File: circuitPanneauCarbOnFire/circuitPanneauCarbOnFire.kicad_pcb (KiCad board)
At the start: 2 copper layers, 13 parts, among them SW1 SW_DIP_x01, SW2 SW_DIP_x01

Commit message: fichier gerber
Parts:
- added ?: MountingHole_2.7mm_M2.5, MountingHole:MountingHole_2.7mm_M2.5, F.Cu at (86.4, 125.7)
- added ?: MountingHole_2.7mm_M2.5, MountingHole:MountingHole_2.7mm_M2.5, F.Cu at (86.4, 86.4)
- added ?: MountingHole_2.7mm_M2.5, MountingHole:MountingHole_2.7mm_M2.5, F.Cu at (119.4, 125.7)
- added ?: MountingHole_2.7mm_M2.5, MountingHole:MountingHole_2.7mm_M2.5, F.Cu at (119.4, 86.4)
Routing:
- net Net-(C1-Pad1): track 46.6 -> 52.0 mm
- net Net-(D1-Pad1): track 47.7 -> 52.3 mm
- net Net-(R1-Pad1): track 56.2 -> 60.1 mm
- net Net-(C1-Pad2): track 40.3 -> 42.5 mm
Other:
- board outline added: 40.6 x 47 mm
- net class Default: clearance 0.2 -> 1; trace_width 0.25 -> 0.5; via_dia 0.8 -> 1
- rule trace_clearance: 0.2 -> 1

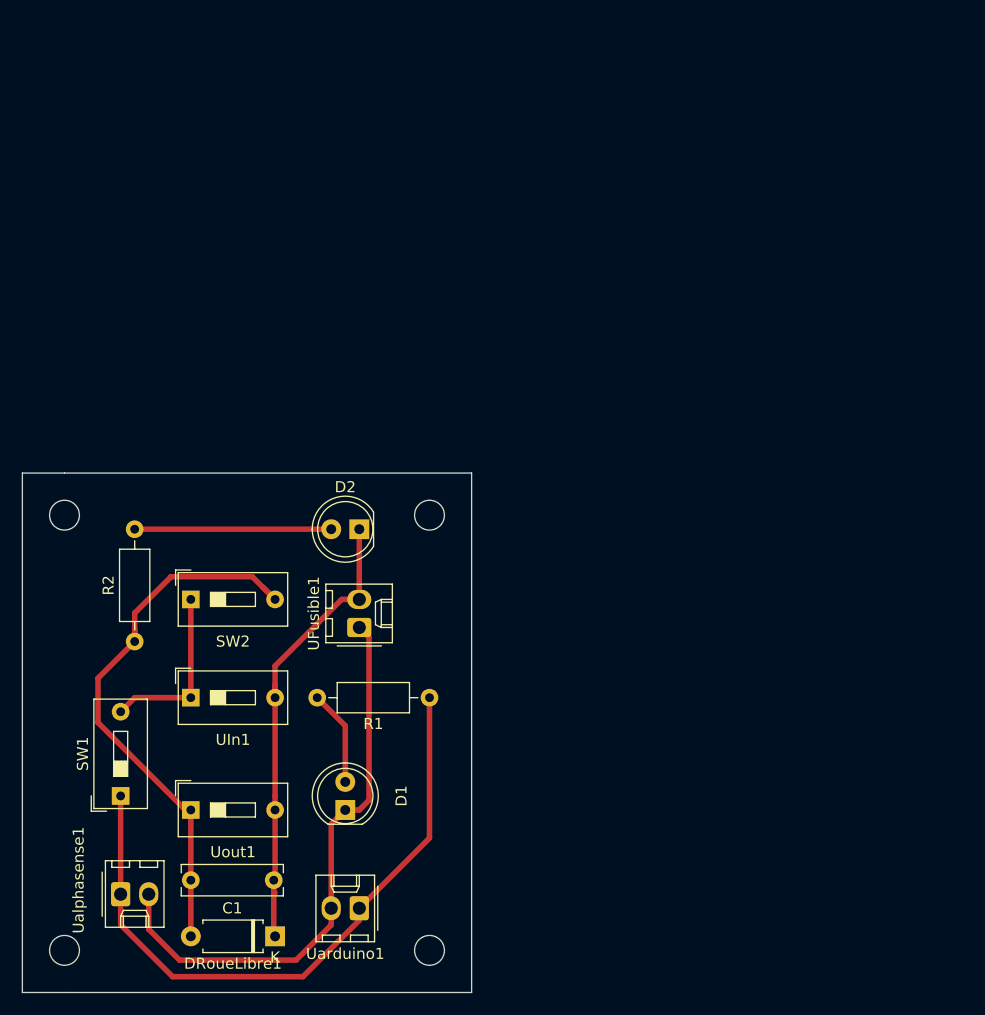
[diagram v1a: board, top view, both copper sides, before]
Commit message: circuit electrique grove+capteur+panneauAvant
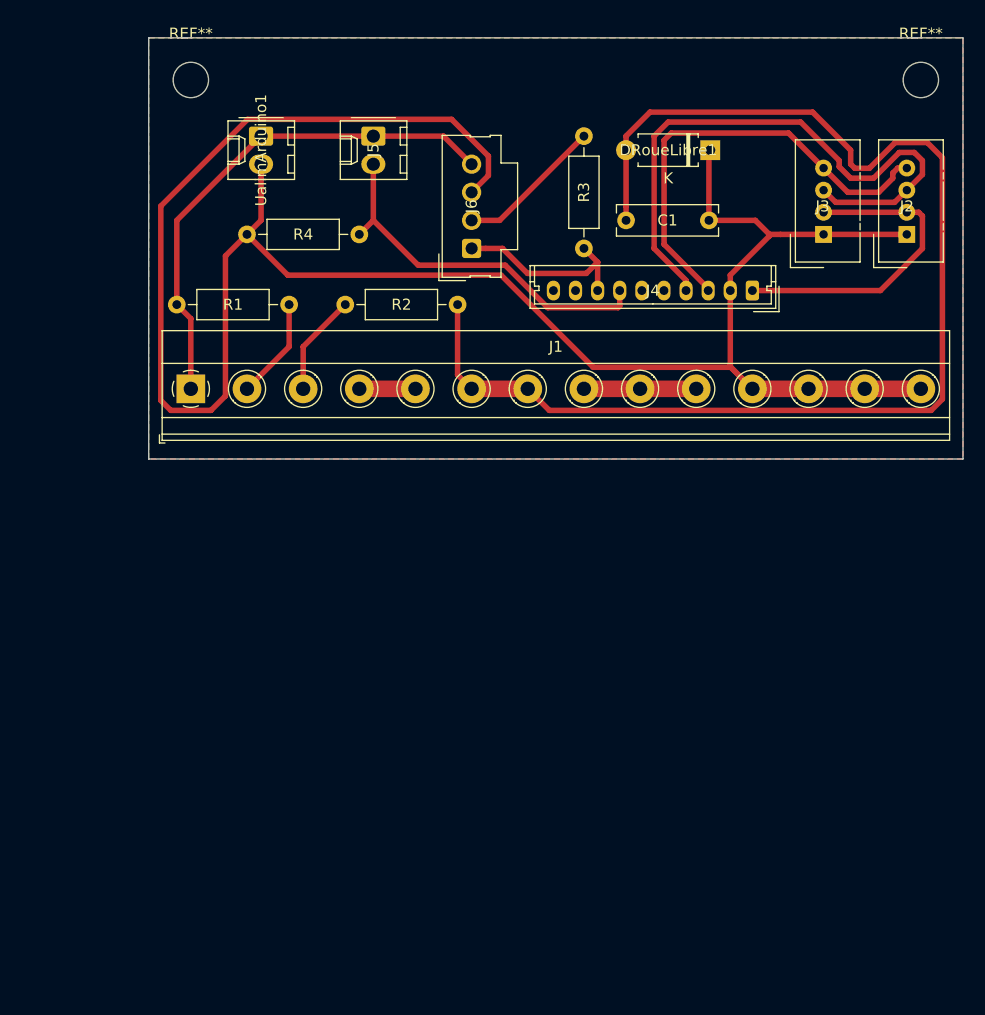
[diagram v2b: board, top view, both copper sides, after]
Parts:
- removed ? (x4): MountingHole_2.7mm_M2.5, MountingHole:MountingHole_2.7mm_M2.5
- removed D1, D2: LED, LED_THT:LED_D5.0mm_IRGrey
- removed SW1, SW2: SW_DIP_x01, Button_Switch_THT:SW_DIP_SPSTx01_Slide_9.78x4.72mm_W7.62mm_P2.54mm
- removed UFusible1, Ualphasense1, Uarduino1: molex2pin, Connector_Molex:Molex_KK-254_AE-6410-02A_1x02_P2.54mm_Vertical
- removed UIn1, Uout1: connecteurCC12V, Button_Switch_THT:SW_DIP_SPSTx01_Slide_9.78x4.72mm_W7.62mm_P2.54mm
- added J1: Screw_Terminal_01x14, TerminalBlock_Phoenix:TerminalBlock_Phoenix_MKDS-1,5-14-5.08_1x14_P5.08mm_Horizontal, F.Cu at (97.8, 74.9)
- added J2: 4P4C, Connector:NS-Tech_Grove_1x04_P2mm_Vertical, F.Cu at (162.6, 61.0)
- added J3: 4P4C, Connector:NS-Tech_Grove_1x04_P2mm_Vertical, F.Cu at (155.0, 61.0)
- added J4: Conn_01x10_Male, Connector_Molex:Molex_Micro-Latch_53253-1070_1x10_P2.00mm_Vertical, F.Cu at (148.6, 66.0)
- added J5: Conn_01x02_Male, Connector_Molex:Molex_KK-254_AE-6410-02A_1x02_P2.54mm_Vertical, F.Cu at (114.3, 52.1)
- added J6: 4P4C, Connector_Molex:Molex_SL_171971-0004_1x04_P2.54mm_Vertical, F.Cu at (123.2, 62.2)
- added R3: 220, Resistor_THT:R_Axial_DIN0207_L6.3mm_D2.5mm_P10.16mm_Horizontal, F.Cu at (133.3, 62.2)
- added R4: 100, Resistor_THT:R_Axial_DIN0207_L6.3mm_D2.5mm_P10.16mm_Horizontal, F.Cu at (113.0, 61.0)
- added REF**: MountingHole_3.2mm_M3, MountingHole:MountingHole_3.2mm_M3, F.Cu at (163.8, 47.0)
- added REF**: MountingHole_3.2mm_M3, MountingHole:MountingHole_3.2mm_M3, F.Cu at (97.8, 47.0)
- added UalimArduino1: molex2pin, Connector_Molex:Molex_KK-254_AE-6410-02A_1x02_P2.54mm_Vertical, F.Cu at (104.1, 52.1)
- moved DRoueLibre1 81.3 mm to (144.8, 53.3)
- moved C1 71.5 mm to (137.2, 59.7)
- moved R1 42.3 mm to (96.5, 67.3), turned to 0 degrees
- moved R2 42.2 mm to (121.9, 67.3), turned to 180 degrees
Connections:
- net Net-(C1-Pad1) renamed SwitchOut2
- net Net-(C1-Pad2) renamed AnoLedIn
- R1 pad 1: Net-(R1-Pad1) -> Fusible1
- R1 pad 2: Net-(D1-Pad2) -> CatLedIn
- R2 pad 2: Net-(D2-Pad2) -> CatLedOut
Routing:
- net AnoLedIn: track 42.5 -> 192.6 mm
- net SwitchOut2: track 52.0 -> 115.3 mm
- net Net-(R1-Pad1): track 60.1 -> 0.00 mm
- net SDA: track 0.00 -> 55.4 mm
- net Net-(D1-Pad1): track 52.3 -> 0.00 mm
- net Fusible1: track 0.00 -> 46.6 mm
- net SCL: track 0.00 -> 40.9 mm
- net A0: track 0.00 -> 33.9 mm
- net Vdd: track 0.00 -> 29.0 mm
- net Net-(D2-Pad2): track 17.8 -> 0.00 mm
- net A1: track 0.00 -> 17.1 mm
- net Net-(SW1-Pad2): track 15.8 -> 0.00 mm
- net Net-(J6-Pad2): track 0.00 -> 13.3 mm
- net SwitchIn1: track 0.00 -> 10.2 mm
- net CatLedOut: track 0.00 -> 9.20 mm
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- added copper zone on F.Cu, net AnoLedIn
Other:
- board size 40.6 x 47 mm -> 73.7 x 38.1 mm
- net class Default: clearance 1 -> 0.4; via_dia 1 -> 0.4; via_drill 0.4 -> 0.3
- rule trace_clearance: 1 -> 0.4
